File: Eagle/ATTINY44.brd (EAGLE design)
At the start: 20.6 x 20.9 mm, 8 parts, among them IC1 TINY85

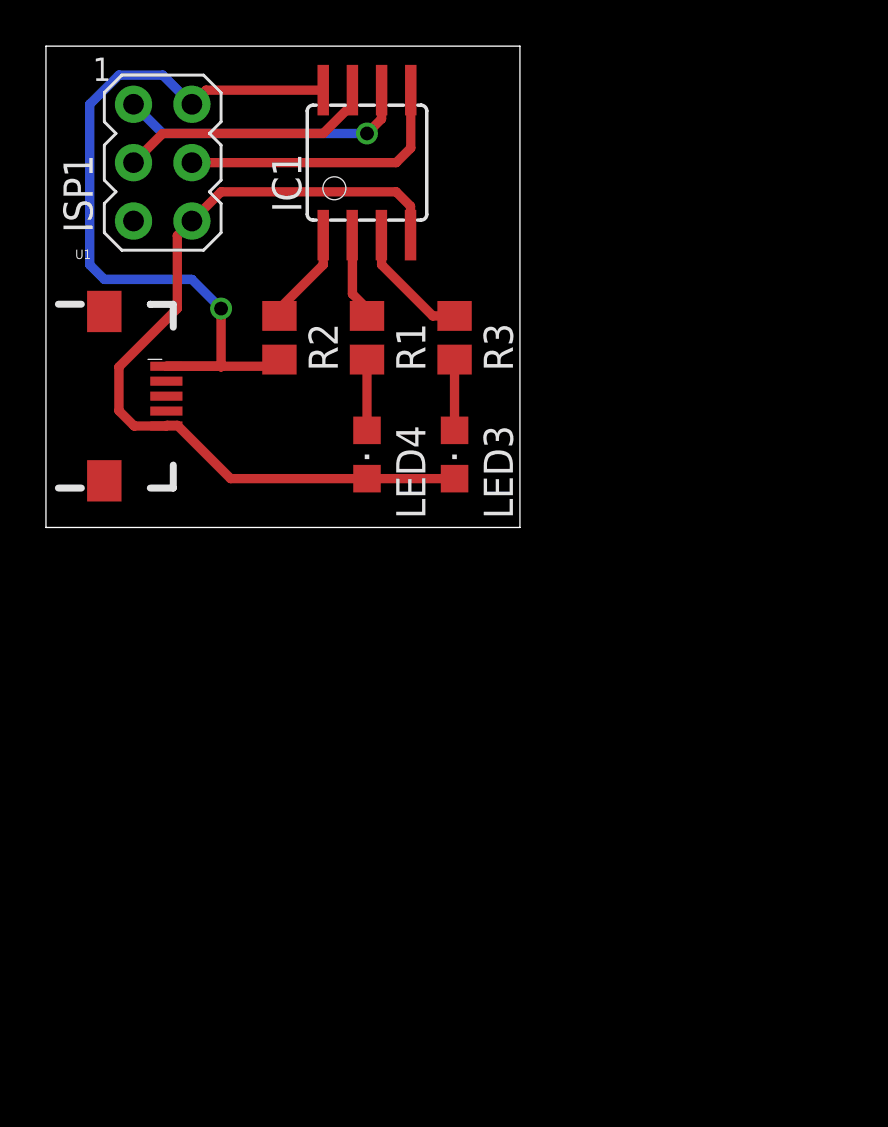
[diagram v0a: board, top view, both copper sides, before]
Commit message: Added ATTINY44 breakout board
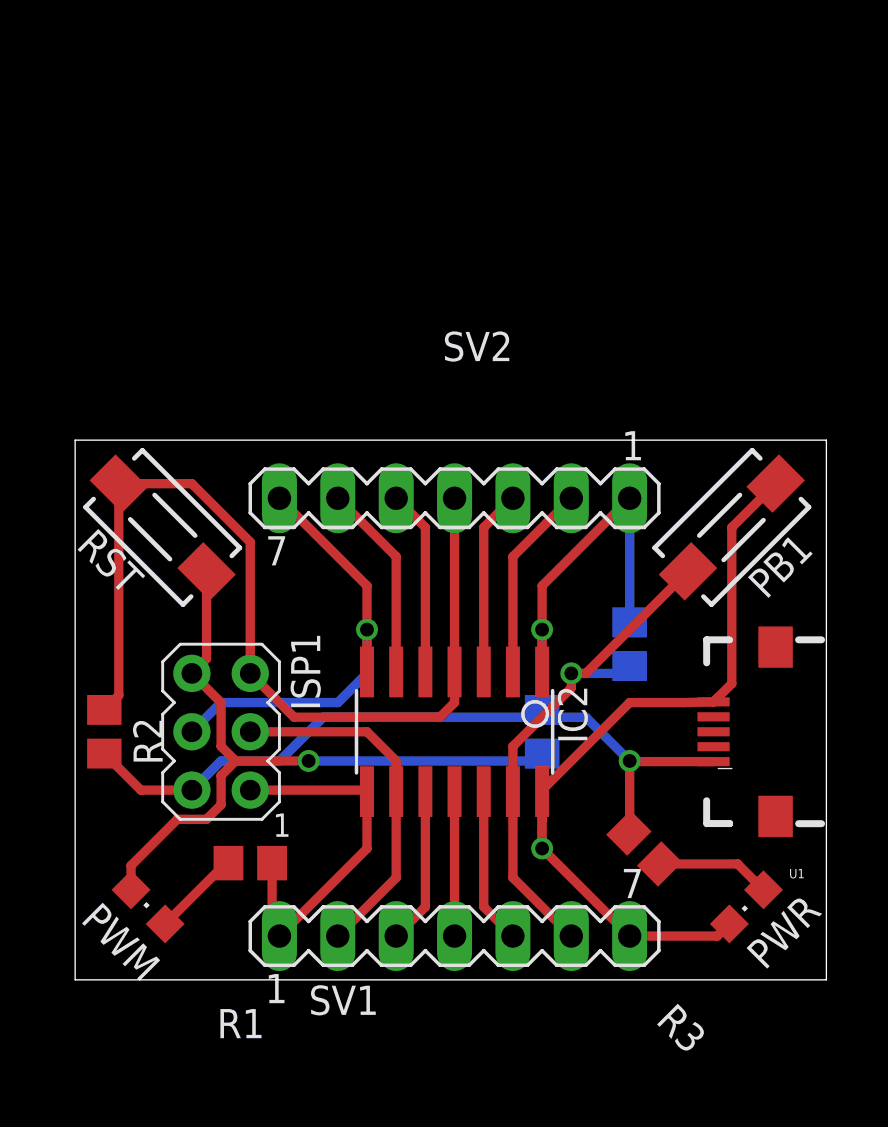
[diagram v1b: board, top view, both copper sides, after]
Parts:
- removed IC1: TINY85, atmel:SOIC8
- removed LED3, LED4: (no value), adafruit:CHIPLED_0805
- added C1: (no value), rcl:C0805
- added IC2: TINY24/44/84-SSU, avr-5:SOIC14
- added PB1: PB1, switch-tact:DTSM-3
- added PWM, PWR: (no value), adafruit:CHIPLED_0805
- added R4: 10K, rcl:R0805
- added RST: RST, switch-tact:DTSM-3
- added SV1, SV2: (no value), con-lstb:MA07-1
- moved U1 32.7 mm to (30.5, 10.8), turned to 180 degrees
- moved ISP1 24.9 mm to (6.35, 10.8), turned to 180 degrees
- moved R3 23.7 mm to (24.8, 5.71), turned to 315 degrees
- moved R1 23.4 mm to (7.62, 5.08), turned to 180 degrees
- moved R2 18.8 mm to (1.27, 10.8)
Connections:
- removed net LED1: IC1.3, R3.1
- removed net LED2: IC1.2, R1.1
- new net N$3: IC2.2, SV2.2
- new net N$4: IC2.3, SV2.3
- new net N$5: IC2.5, SV2.5
- new net N$6: IC2.6, SV2.6
- new net PIN10: IC2.10, SV1.3
- new net PIN11: IC2.11, SV1.4
- new net PIN12: IC2.12, SV1.5
- new net PIN13: IC2.13, PB1.1, R4.1, SV1.6
- net GND: now also C1.2, IC2.14, PB1.2, PWM.C, PWR.C, RST.2, SV1.7; no longer IC1.4, LED3.C, LED4.C
- net MISO: now also IC2.8, R1.1, SV1.1; no longer IC1.6
- net MOSI: now also IC2.7, SV2.7; no longer IC1.5
- net N$1: now also PWR.A; no longer LED3.A
- net N$2: now also PWM.A; no longer LED4.A
- net RST: now also IC2.4, RST.1, SV2.4; no longer IC1.1
- net SCK: now also IC2.9, SV1.2; no longer IC1.7
- net VCC: now also C1.1, IC2.1, R3.1, R4.2, SV2.1; no longer IC1.8
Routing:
- net RST: track 4.31 -> 42.1 mm
- net GND: track 37.0 -> 70.2 mm, vias 0 -> 2
- net PIN13: track 0.00 -> 23.1 mm, vias 0 -> 1
- net VCC: track 35.1 -> 51.0 mm, vias 1 -> 2
- net N$6: track 0.00 -> 8.61 mm
- net N$3: track 0.00 -> 8.61 mm
- net N$5: track 0.00 -> 8.08 mm
- net N$4: track 0.00 -> 8.08 mm
- net MOSI: track 12.3 -> 19.7 mm, vias 0 -> 1
- net PIN12: track 0.00 -> 6.81 mm
- net PIN10: track 0.00 -> 6.81 mm
- net PIN11: track 0.00 -> 6.29 mm
- net LED1: track 5.39 -> 0.00 mm
- net SCK: track 11.2 -> 15.5 mm
- net LED2: track 3.78 -> 0.00 mm
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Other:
- board size 20.6 x 20.9 mm -> 32.7 x 23.5 mm

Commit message: added code section
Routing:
- net GND: track 70.2 -> 0.00 mm, vias 2 -> 0
- added copper zone on layer 1, net GND
- added copper zone on layer 16, net GND
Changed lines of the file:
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@@
 </class>
 </classes>
-<designrules name="LaenPCBOrder">
+<designrules name="OSHParkDRC">
 <description language="de">&lt;b&gt;EAGLE Design Rules&lt;/b&gt;
 &lt;p&gt;
@@
 <contactref element="ISP1" pad="6"/>
 <contactref element="SV1" pad="7"/>
-<wire x1="20.32" y1="9.525" x2="20.32" y2="6.985" width="0.4064" layer="16"/>
-<wire x1="5.08" y1="13.335" x2="6.35" y2="12.065" width="0.4064" layer="1"/>
-<wire x1="6.35" y1="12.065" x2="6.35" y2="10.16" width="0.4064" layer="1"/>
-<wire x1="6.35" y1="10.16" x2="6.985" y2="9.525" width="0.4064" layer="1"/>
-<wire x1="6.985" y1="9.525" x2="10.16" y2="9.525" width="0.4064" layer="1"/>
-<via x="10.16" y="9.525" extent="1-16" drill="0.6"/>
-<wire x1="10.16" y1="9.525" x2="20.32" y2="9.525" width="0.4064" layer="16"/>
-<wire x1="20.32" y1="9.525" x2="20.32" y2="9.845" width="0.4064" layer="16"/>
-<wire x1="27.78" y1="12.095" x2="26.48" y2="12.065" width="0.4064" layer="1"/>
-<wire x1="26.48" y1="12.065" x2="24.13" y2="12.065" width="0.4064" layer="1"/>
-<wire x1="24.13" y1="12.065" x2="20.32" y2="8.255" width="0.4064" layer="1"/>
-<wire x1="20.32" y1="8.255" x2="20.32" y2="8.1915" width="0.4064" layer="1"/>
 <contactref element="RST" pad="2"/>
 <contactref element="PWR" pad="C"/>
-<wire x1="24.13" y1="1.905" x2="20.32" y2="5.715" width="0.4064" layer="1"/>
-<wire x1="20.32" y1="8.1915" x2="20.32" y2="5.715" width="0.4064" layer="1"/>
-<via x="20.32" y="5.715" extent="1-16" drill="0.6"/>
-<wire x1="20.32" y1="5.715" x2="20.32" y2="9.845" width="0.4064" layer="16"/>
 <contactref element="PB1" pad="2"/>
-<wire x1="6.985" y1="9.525" x2="6.35" y2="8.89" width="0.4064" layer="1"/>
-<wire x1="6.35" y1="8.89" x2="6.35" y2="7.62" width="0.4064" layer="1"/>
-<wire x1="6.35" y1="7.62" x2="5.715" y2="6.985" width="0.4064" layer="1"/>
-<wire x1="5.715" y1="6.985" x2="4.445" y2="6.985" width="0.4064" layer="1"/>
-<wire x1="27.9441875" y1="12.2591875" x2="27.78" y2="12.095" width="0.4064" layer="1"/>
-<wire x1="30.4841875" y1="21.5941875" x2="28.575" y2="19.685" width="0.4064" layer="1"/>
-<wire x1="28.575" y1="19.685" x2="28.575" y2="12.89" width="0.4064" layer="1"/>
-<wire x1="28.575" y1="12.89" x2="27.78" y2="12.095" width="0.4064" layer="1"/>
-<wire x1="5.7191875" y1="17.775809375" x2="5.7191875" y2="13.9741875" width="0.4064" layer="1"/>
-<wire x1="5.7191875" y1="13.9741875" x2="5.08" y2="13.335" width="0.4064" layer="1"/>
-<wire x1="24.13" y1="1.905" x2="27.94" y2="1.905" width="0.4064" layer="1"/>
-<wire x1="27.94" y1="1.905" x2="28.4675375" y2="2.4325375" width="0.4064" layer="1"/>
-<wire x1="4.445" y1="6.985" x2="2.4325375" y2="4.9725375" width="0.4064" layer="1"/>
-<wire x1="2.4325375" y1="4.9725375" x2="2.4325375" y2="3.917459375" width="0.4064" layer="1"/>
+<polygon width="0.4064" layer="1">
+<vertex x="0" y="22.86"/>
+<vertex x="0" y="0"/>
+<vertex x="32.385" y="0"/>
+<vertex x="32.385" y="23.495"/>
+<vertex x="0" y="23.495"/>
+</polygon>
+<polygon width="0.4064" layer="16">
+<vertex x="33.02" y="0"/>
+<vertex x="0" y="0"/>
+<vertex x="0" y="20.32"/>
+<vertex x="0" y="22.86"/>
+<vertex x="33.02" y="22.86"/>
+</polygon>
 </signal>
 <signal name="N$1">
